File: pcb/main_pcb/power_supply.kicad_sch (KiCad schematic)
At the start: 34 parts, among them J12 Screw_Terminal_01x02, J13 Conn_01x02_Male, Q1 Q_PMOS_GDS, SW1 SW_SPDT, U4 LM1117-3.3, U5 TPIC74101

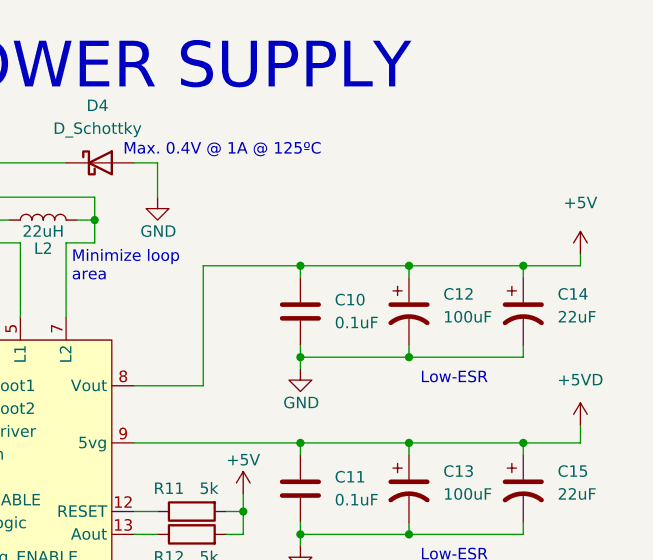
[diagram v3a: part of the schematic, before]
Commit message: Complete digital routing
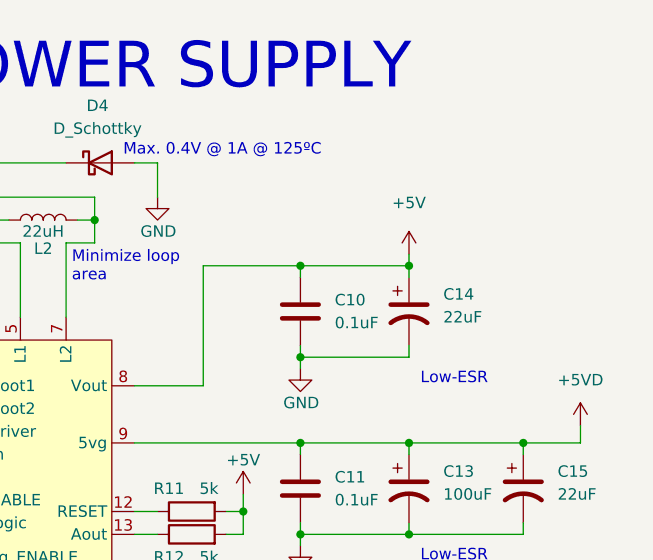
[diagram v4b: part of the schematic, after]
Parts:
- removed C12: 100uF, Capacitor_SMD:CP_Elec_8x10.5, symbol Device:C_Polarized_US
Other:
- moved on the sheet: C14
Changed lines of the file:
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@@
   (junction (at 67.31 59.69) (diameter 0) (color 0 0 0 0)
   )
-  (junction (at 238.125 51.435) (diameter 0) (color 0 0 0 0)
-  )
   (junction (at 197.485 90.17) (diameter 0) (color 0 0 0 0)
   )
@@
   )
   (junction (at 100.965 154.94) (diameter 0) (color 0 0 0 0)
-  )
-  (junction (at 225.425 61.595) (diameter 0) (color 0 0 0 0)
   )
   (junction (at 225.425 51.435) (diameter 0) (color 0 0 0 0)
@@
     (stroke (width 0) (type default) (color 0 0 0 0))
   )
-  (wire (pts (xy 244.475 50.165) (xy 244.475 51.435))
+  (wire (pts (xy 225.425 50.165) (xy 225.425 51.435))
     (stroke (width 0) (type default) (color 0 0 0 0))
   )
@@
     (stroke (width 0) (type default) (color 0 0 0 0))
   )
-  (wire (pts (xy 238.125 52.705) (xy 238.125 51.435))
-    (stroke (width 0) (type default) (color 0 0 0 0))
-  )
   (wire (pts (xy 194.945 64.77) (xy 202.565 64.77))
     (stroke (width 0) (type default) (color 0 0 0 0))
@@
     (stroke (width 0) (type default) (color 0 0 0 0))
   )
-  (wire (pts (xy 244.475 51.435) (xy 238.125 51.435))
-    (stroke (width 0) (type default) (color 0 0 0 0))
-  )
   (wire (pts (xy 170.815 91.44) (xy 174.625 91.44))
     (stroke (width 0) (type default) (color 0 0 0 0))
@@
     (stroke (width 0) (type default) (color 0 0 0 0))
   )
-  (wire (pts (xy 225.425 51.435) (xy 238.125 51.435))
-    (stroke (width 0) (type default) (color 0 0 0 0))
-  )
   (wire (pts (xy 154.305 96.52) (xy 154.305 98.425))
     (stroke (width 0) (type default) (color 0 0 0 0))
@@
     (stroke (width 0) (type default) (color 0 0 0 0))
   )
-  (wire (pts (xy 238.125 61.595) (xy 225.425 61.595))
-    (stroke (width 0) (type default) (color 0 0 0 0))
-  )
   (wire (pts (xy 140.97 83.82) (xy 140.97 88.9))
     (stroke (width 0) (type default) (color 0 0 0 0))
   )
-  (wire (pts (xy 238.125 60.325) (xy 238.125 61.595))
-    (stroke (width 0) (type default) (color 0 0 0 0))
-  )
   (wire (pts (xy 163.83 57.785) (xy 163.83 67.31))
     (stroke (width 0) (type default) (color 0 0 0 0))
@@
     (stroke (width 0) (type default) (color 0 0 0 0))
   )
-  (wire (pts (xy 213.36 51.435) (xy 202.565 51.435))
+  (wire (pts (xy 202.565 51.435) (xy 213.36 51.435))
     (stroke (width 0) (type default) (color 0 0 0 0))
   )
@@
     (pin "1")
   )
-  (symbol (lib_id "Device:C_Polarized_US") (at 225.425 56.515 0) (unit 1)
-    (in_bom yes) (on_board yes) (fields_autoplaced)
-    (property "Reference" "C12" (id 0) (at 229.235 54.6099 0)
-      (effects (font (size 1.27 1.27)) (justify left))
-    )
-    (property "Value" "100uF" (id 1) (at 229.235 57.1499 0)
-      (effects (font (size 1.27 1.27)) (justify left))
-    )
-    (property "Footprint" "Capacitor_SMD:CP_Elec_8x10.5" (id 2) (at 225.425 56.515 0)
-      (effects (font (size 1.27 1.27)) hide)
-    )
-    (property "Datasheet" "~" (id 3) (at 225.425 56.515 0)
-      (effects (font (size 1.27 1.27)) hide)
-    )
-    (pin "1")
-    (pin "2")
-  )
   (symbol (lib_id "Device:L") (at 104.14 43.815 90) (unit 1)
     (in_bom yes) (on_board yes)
@@
     (pin "3")
   )
-  (symbol (lib_id "Device:C_Polarized_US") (at 238.125 56.515 0) (unit 1)
-    (in_bom yes) (on_board yes) (fields_autoplaced)
-    (property "Reference" "C14" (id 0) (at 241.935 54.6099 0)
-      (effects (font (size 1.27 1.27)) (justify left))
-    )
-    (property "Value" "22uF" (id 1) (at 241.935 57.1499 0)
-      (effects (font (size 1.27 1.27)) (justify left))
-    )
-    (property "Footprint" "Capacitor_SMD:CP_Elec_8x10.5" (id 2) (at 238.125 56.515 0)
-      (effects (font (size 1.27 1.27)) hide)
-    )
-    (property "Datasheet" "~" (id 3) (at 238.125 56.515 0)
+  (symbol (lib_id "Device:C_Polarized_US") (at 225.425 56.515 0) (unit 1)
+    (in_bom yes) (on_board yes) (fields_autoplaced)
+    (property "Reference" "C14" (id 0) (at 229.235 54.6099 0)
+      (effects (font (size 1.27 1.27)) (justify left))
+    )
+    (property "Value" "22uF" (id 1) (at 229.235 57.1499 0)
+      (effects (font (size 1.27 1.27)) (justify left))
+    )
+    (property "Footprint" "Capacitor_SMD:CP_Elec_8x10.5" (id 2) (at 225.425 56.515 0)
+      (effects (font (size 1.27 1.27)) hide)
+    )
+    (property "Datasheet" "~" (id 3) (at 225.425 56.515 0)
       (effects (font (size 1.27 1.27)) hide)
     )
@@
     (pin "2")
   )
-  (symbol (lib_id "power:+5V") (at 244.475 50.165 0) (unit 1)
-    (in_bom yes) (on_board yes) (fields_autoplaced)
-    (property "Reference" "#PWR047" (id 0) (at 244.475 53.975 0)
-      (effects (font (size 1.27 1.27)) hide)
-    )
-    (property "Value" "+5V" (id 1) (at 244.475 44.45 0))
-    (property "Footprint" "" (id 2) (at 244.475 50.165 0)
-      (effects (font (size 1.27 1.27)) hide)
-    )
-    (property "Datasheet" "" (id 3) (at 244.475 50.165 0)
-      (effects (font (size 1.27 1.27)) hide)
-    )
+  (symbol (lib_id "power:+5V") (at 225.425 50.165 0) (unit 1)
+    (in_bom yes) (on_board yes) (fields_autoplaced)
+    (property "Reference" "#PWR047" (id 0) (at 225.425 53.975 0)
+      (effects (font (size 1.27 1.27)) hide)
+    )
+    (property "Value" "+5V" (id 1) (at 225.425 44.45 0))
+    (property "Footprint" "" (id 2) (at 225.425 50.165 0)
+      (effects (font (size 1.27 1.27)) hide)
+    )
+    (property "Datasheet" "" (id 3) (at 225.425 50.165 0)
+      (effects (font (size 1.27 1.27)) hide)
+    )

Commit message: More routing
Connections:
- net GND: now also U5.21 (PAD)
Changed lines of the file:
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@@
     (pin "2")
     (pin "20")
+    (pin "21")
     (pin "3")
     (pin "4")

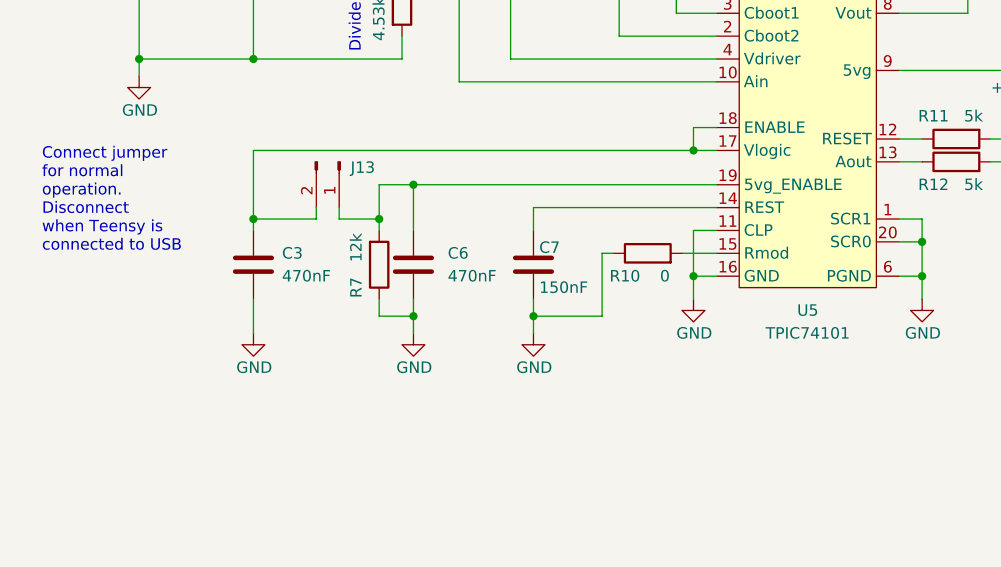
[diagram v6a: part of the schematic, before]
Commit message: Fix many DRC errors; correct motor B sig names
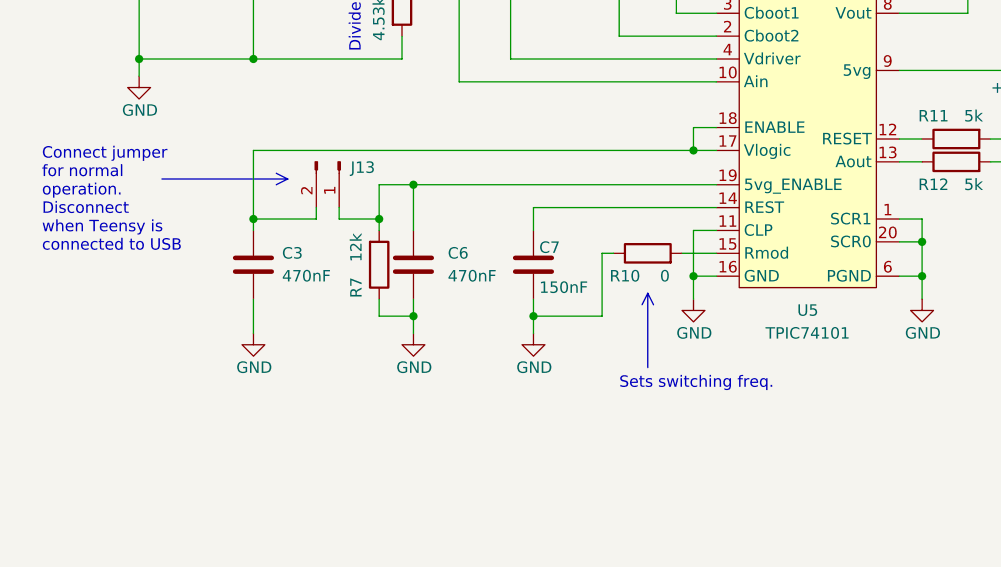
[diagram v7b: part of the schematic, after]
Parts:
- U5: footprint Package_SO:HTSSOP-20-1EP_4.4x6.5mm_P0.65mm_EP3.4x6.5mm_ThermalVias -> custom_footprints:HTSSOP-20-1EP_4.4x6.5mm_P0.65mm_EP3.4x6.5mm_ThermalVias
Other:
- note added: "Sets switching freq."
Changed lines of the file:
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@@
     (stroke (width 0) (type default) (color 0 0 0 0))
+  )
+  (polyline (pts (xy 127 83.185) (xy 125.73 82.55))
+    (stroke (width 0) (type solid) (color 0 0 0 0))
   )
   (wire (pts (xy 100.965 154.94) (xy 113.665 154.94))
@@
     (stroke (width 0) (type default) (color 0 0 0 0))
   )
+  (polyline (pts (xy 167.005 95.885) (xy 167.64 97.155))
+    (stroke (width 0) (type solid) (color 0 0 0 0))
+  )
   (wire (pts (xy 225.425 60.325) (xy 225.425 61.595))
     (stroke (width 0) (type default) (color 0 0 0 0))
@@
     (stroke (width 0) (type default) (color 0 0 0 0))
   )
+  (polyline (pts (xy 167.005 95.885) (xy 167.005 104.14))
+    (stroke (width 0) (type solid) (color 0 0 0 0))
+  )
   (wire (pts (xy 182.245 48.895) (xy 179.07 48.895))
     (stroke (width 0) (type default) (color 0 0 0 0))
@@
     (stroke (width 0) (type default) (color 0 0 0 0))
   )
+  (polyline (pts (xy 167.005 95.885) (xy 166.37 97.155))
+    (stroke (width 0) (type solid) (color 0 0 0 0))
+  )
   (wire (pts (xy 197.485 93.98) (xy 197.485 96.52))
     (stroke (width 0) (type default) (color 0 0 0 0))
@@
     (stroke (width 0) (type default) (color 0 0 0 0))
   )
+  (polyline (pts (xy 127 83.185) (xy 113.03 83.185))
+    (stroke (width 0) (type solid) (color 0 0 0 0))
+  )
   (wire (pts (xy 238.125 80.01) (xy 238.125 81.28))
     (stroke (width 0) (type default) (color 0 0 0 0))
@@
   (wire (pts (xy 187.325 48.895) (xy 190.5 48.895))
     (stroke (width 0) (type default) (color 0 0 0 0))
+  )
+  (polyline (pts (xy 127 83.185) (xy 125.73 83.82))
+    (stroke (width 0) (type solid) (color 0 0 0 0))
   )
   (wire (pts (xy 213.36 71.12) (xy 225.425 71.12))
@@
   (text "DIGITAL 5V POWER SUPPLY" (at 130.175 32.385 0)
     (effects (font (size 5.08 5.08)) (justify left bottom))
+  )
+  (text "Sets switching freq." (at 163.83 106.68 0)
+    (effects (font (size 1.27 1.27)) (justify left bottom))
   )
   (text "Low-ESR" (at 226.695 84.455 0)
@@
     (property "Reference" "U5" (id 0) (at 184.785 97.79 0))
     (property "Value" "TPIC74101" (id 1) (at 184.785 100.33 0))
-    (property "Footprint" "Package_SO:HTSSOP-20-1EP_4.4x6.5mm_P0.65mm_EP3.4x6.5mm_ThermalVias" (id 2) (at 184.785 77.47 0)
-      (effects (font (size 1.27 1.27)) hide)
-    )
+    (property "Footprint" "custom_footprints:HTSSOP-20-1EP_4.4x6.5mm_P0.65mm_EP3.4x6.5mm_ThermalVias" (id 2) (at 184.785 77.47 0)
+      (effects (font (size 1.27 1.27)) hide)
+    )

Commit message: Change 3V3 reg reverse diode footprint
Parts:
- D3: footprint Diode_SMD:D_SOD-110 -> Diode_SMD:D_0805_2012Metric
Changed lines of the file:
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@@
     (property "Reference" "D3" (id 0) (at 86.36 135.89 0))
     (property "Value" "D" (id 1) (at 86.36 138.43 0))
-    (property "Footprint" "Diode_SMD:D_SOD-110" (id 2) (at 86.36 142.24 0)
+    (property "Footprint" "Diode_SMD:D_0805_2012Metric" (id 2) (at 86.36 142.24 0)
       (effects (font (size 1.27 1.27)) hide)
     )
